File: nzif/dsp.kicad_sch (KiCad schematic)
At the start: 64 parts, among them U207 ADAU1467WBCPZ300

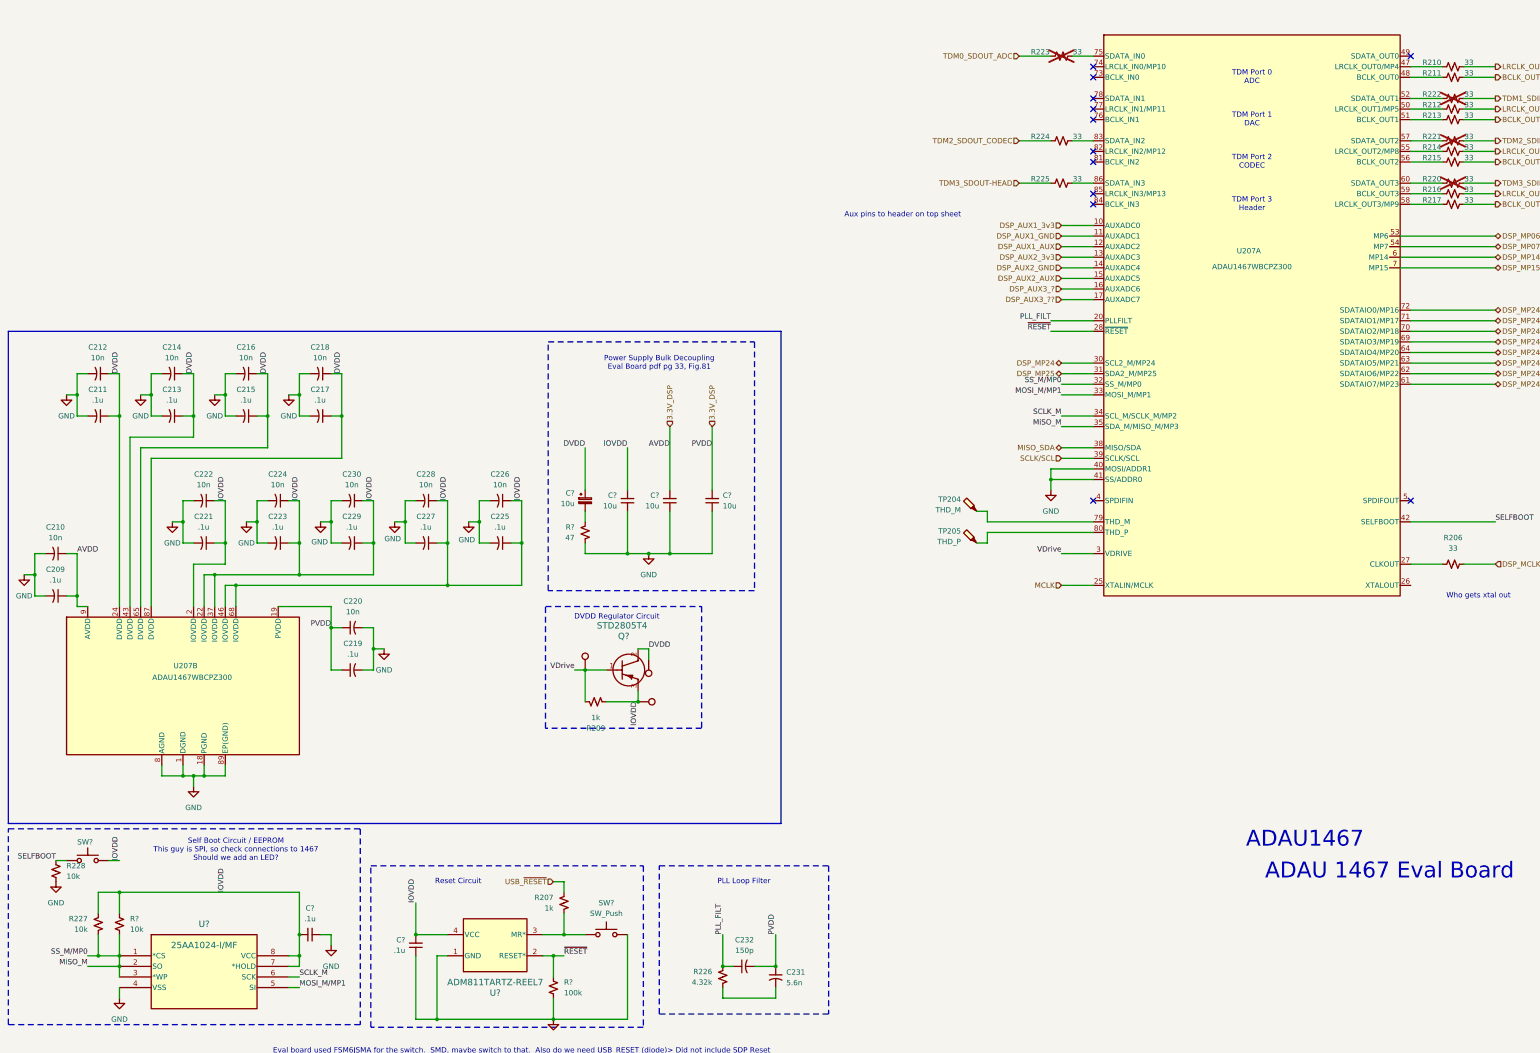
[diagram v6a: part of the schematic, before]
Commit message: updated adau1467 symbol
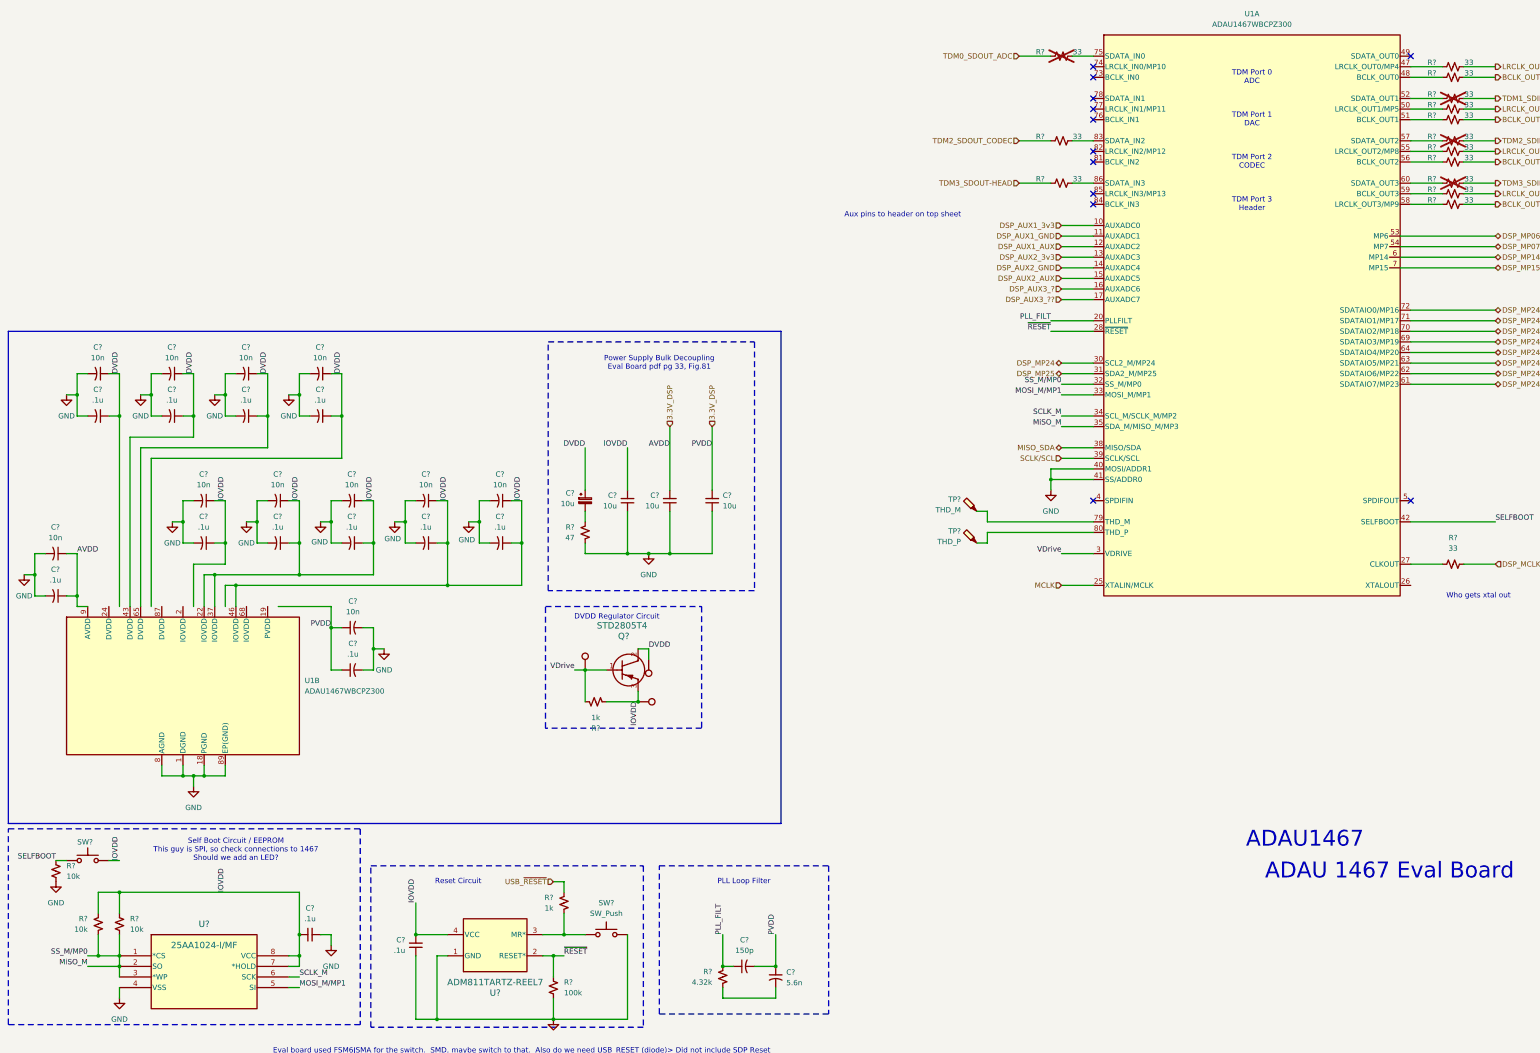
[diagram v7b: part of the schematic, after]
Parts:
- removed U207: ADAU1467WBCPZ300, nzif_footprints:CP_88_10_ADI, symbol nzif_radio_symbol_library:ADAU1467WBCPZ300
- added U1: ADAU1467WBCPZ300, nzif_footprints:CP_88_10_ADI, symbol nzif_radio_symbol_library:ADAU1467WBCPZ300
- renumbered C219 to C?, C222 to C?, C221 to C?, C210 to C?, C214 to C?, C218 to C?, C209 to C?, C231 to C?, C217 to C?, C227 to C?, C225 to C?, C220 to C?, C229 to C?, C223 to C?, C226 to C?, C213 to C?, C211 to C?, C228 to C?, C212 to C?, C215 to C?, C230 to C?, C224 to C?, C232 to C?, C216 to C?, R210 to R?, R207 to R?, R209 to R?, R217 to R?, R225 to R?, R220 to R?, R206 to R?, R224 to R?, R214 to R?, R212 to R?, R215 to R?, R221 to R?, R228 to R?, R213 to R?, R226 to R?, R222 to R?, R216 to R?, R227 to R?, R223 to R?, R211 to R?, TP204 to TP?, TP205 to TP?, TP201 to TP?, TP202 to TP?, TP203 to TP?
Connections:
- net 3.3V_DSP: now also U1.9 (AVDD)
- net DGND: now also U1.1 (DGND), U1.18 (PGND), U1.21 (DGND), U1.23 (DGND), U1.29 (DGND), U1.36 (DGND), U1.40 (MOSI/ADDR1), U1.41 (SS/ADDR0), U1.44 (DGND), U1.45 (DGND), U1.66 (DGND), U1.67 (DGND), U1.8 (AGND), U1.88 (DGND), U1.89 (EP(GND))
- net DSP_AUX1_3v3: now also U1.10 (AUXADC0)
- net DSP_AUX1_AUX: now also U1.12 (AUXADC2)
- net DSP_AUX1_GND: now also U1.11 (AUXADC1)
- net DSP_AUX2_3v3: now also U1.13 (AUXADC3)
- net DSP_AUX2_AUX: now also U1.15 (AUXADC5)
- net DSP_AUX2_GND: now also U1.14 (AUXADC4)
- net DSP_AUX3_?: now also U1.16 (AUXADC6)
- net DSP_AUX3_??: now also U1.17 (AUXADC7)
- net DSP_MP06: now also U1.53 (MP6)
- net DSP_MP07: now also U1.54 (MP7)
- net DSP_MP14: now also U1.6 (MP14)
- net DSP_MP15: now also U1.7 (MP15)
- net DSP_MP24: now also U1.30 (SCL2_M/MP24), U1.61 (SDATAIO7/MP23), U1.62 (SDATAIO6/MP22), U1.63 (SDATAIO5/MP21), U1.64 (SDATAIO4/MP20), U1.69 (SDATAIO3/MP19), U1.70 (SDATAIO2/MP18), U1.71 (SDATAIO1/MP17), U1.72 (SDATAIO0/MP16)
- net DSP_MP25: now also U1.31 (SDA2_M/MP25)
- net DVDD: now also U1.43 (DVDD), U1.65 (DVDD)
- net IOVDD: now also U1.22 (IOVDD), U1.37 (IOVDD), U1.46 (IOVDD)
- net MCLK: now also U1.25 (XTALIN/MCLK)
- net MISO_SDA: now also U1.38 (MISO/SDA)
- net MOSI_M/MP1: now also U1.33 (MOSI_M/MP1)
- net MiSO_M: now also U1.32 (SS_M/MP0), U1.35 (SDA_M/MISO_M/MP3)
- net PLL_FILT: now also U1.20 (PLLFILT)
- net SCLK_M: now also U1.34 (SCL_M/SCLK_M/MP2)
- net SCLK/SCL: now also U1.39 (SCLK/SCL)
- net SELFBOOT: now also U1.42 (SELFBOOT)
- net VDrive: now also U1.3 (VDRIVE)
- net ~{RESET}: now also U1.28 (~{RESET})
- net at R?.2: now also U1.47 (LRCLK_OUT0/MP4)
- net at R?.2: now also U1.58 (LRCLK_OUT3/MP9)
- net at R?.1: now also U1.86 (SDATA_IN3)
- net at R?.2: now also U1.60 (SDATA_OUT3)
- net at TP?.1: now also U1.79 (THD_M)
- net at R?.1: now also U1.27 (CLKOUT)
- net at R?.1: now also U1.83 (SDATA_IN2)
- net at TP?.1: now also U1.80 (THD_P)
- net at R?.2: now also U1.55 (LRCLK_OUT2/MP8)
- net at R?.2: now also U1.50 (LRCLK_OUT1/MP5)
- net at R?.2: now also U1.56 (BCLK_OUT2)
- net at R?.2: now also U1.57 (SDATA_OUT2)
- net at R?.2: now also U1.51 (BCLK_OUT1)
- net at R?.2: now also U1.52 (SDATA_OUT1)
- net at R?.2: now also U1.59 (BCLK_OUT3)
- net at R?.1: now also U1.75 (SDATA_IN0)
- net at R?.2: now also U1.48 (BCLK_OUT0)

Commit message: correct issue with unit a and b of 1467
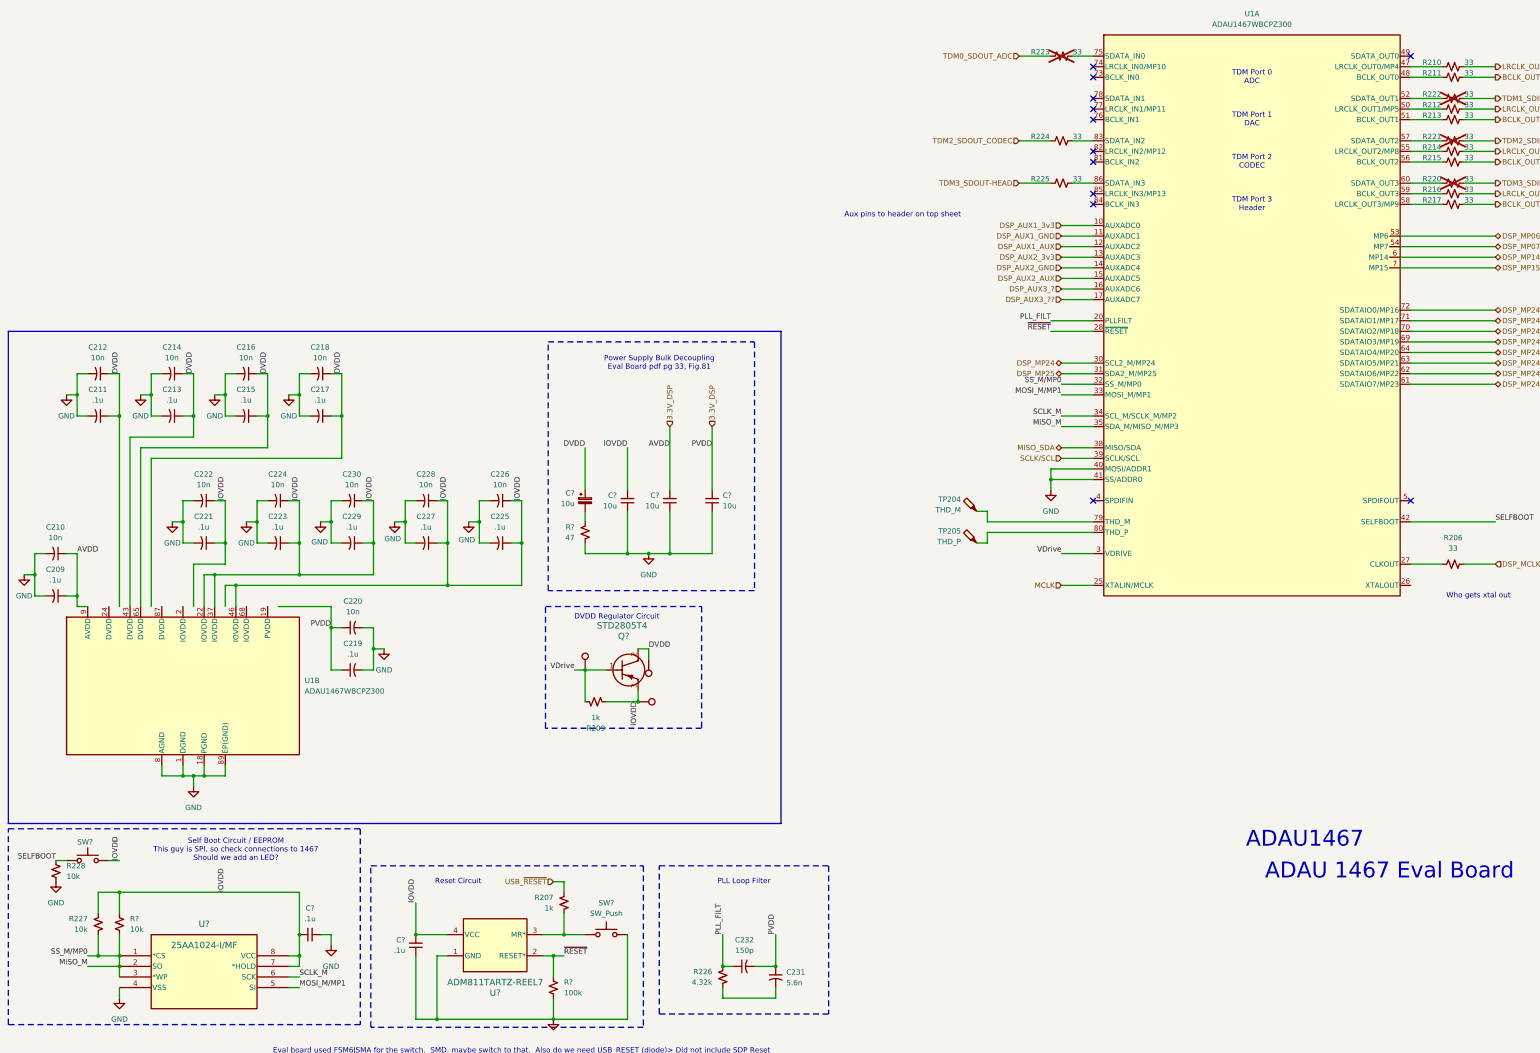
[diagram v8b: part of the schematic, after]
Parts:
- gave numbers to parts that had none: 49
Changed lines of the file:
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@@
 		(dnp no)
 		(fields_autoplaced yes)
-		(property "Reference" "C?"
+		(property "Reference" "C219"
 			(at 96.647 173.99 90)
 			(effects
@@
 		(on_board yes)
 		(dnp no)
-		(property "Reference" "R?"
+		(property "Reference" "R210"
 			(at 355.6 34.544 90)
 			(effects
@@
 		(dnp no)
 		(fields_autoplaced yes)
-		(property "Reference" "C?"
+		(property "Reference" "C222"
 			(at 60.833 133.35 90)
 			(effects
@@
 		(dnp no)
 		(fields_autoplaced yes)
-		(property "Reference" "C?"
+		(property "Reference" "C221"
 			(at 60.833 143.51 90)
 			(effects
@@
 		(on_board yes)
 		(dnp no)
-		(property "Reference" "R?"
+		(property "Reference" "R207"
 			(at 144.78 234.9499 0)
 			(effects
@@
 		(dnp no)
 		(fields_autoplaced yes)
-		(property "Reference" "#PWR?"
+		(property "Reference" "#PWR0213"
 			(at 81.28 120.65 0)
 			(effects
@@
 		(on_board yes)
 		(dnp no)
-		(property "Reference" "R?"
+		(property "Reference" "R209"
 			(at 154.94 194.31 90)
 			(effects
@@
 		(on_board yes)
 		(dnp no)
-		(property "Reference" "R?"
+		(property "Reference" "R217"
 			(at 355.6 67.564 90)
 			(effects
@@
 		(on_board yes)
 		(dnp no)
-		(property "Reference" "R?"
+		(property "Reference" "R225"
 			(at 261.62 62.484 90)
 			(effects
@@
 		(on_board yes)
 		(dnp yes)
-		(property "Reference" "R?"
+		(property "Reference" "R220"
 			(at 355.6 62.484 90)
 			(effects
@@
 		(on_board yes)
 		(dnp no)
-		(property "Reference" "TP?"
+		(property "Reference" "TP204"
 			(at 242.57 139.3824 0)
 			(effects
@@
 		(dnp no)
 		(fields_autoplaced yes)
-		(property "Reference" "C?"
+		(property "Reference" "C210"
 			(at 25.273 146.05 90)
 			(effects
@@
 		(dnp no)
 		(fields_autoplaced yes)
-		(property "Reference" "#PWR?"
+		(property "Reference" "#PWR0210"
 			(at 27.94 120.65 0)
 			(effects
@@
 		(dnp no)
 		(fields_autoplaced yes)
-		(property "Reference" "R?"
+		(property "Reference" "R206"
 			(at 360.68 148.59 90)
 			(effects
@@
 		(on_board yes)
 		(dnp no)
-		(property "Reference" "#PWR?"
+		(property "Reference" "#PWR0219"
 			(at 88.9 151.13 0)
 			(effects
@@
 		(dnp no)
 		(fields_autoplaced yes)
-		(property "Reference" "C?"
+		(property "Reference" "C214"
 			(at 53.213 102.87 90)
 			(effects
@@
 		(dnp no)
 		(fields_autoplaced yes)
-		(property "Reference" "C?"
+		(property "Reference" "C218"
 			(at 88.773 102.87 90)
 			(effects
@@
 		(dnp no)
 		(fields_autoplaced yes)
-		(property "Reference" "C?"
+		(property "Reference" "C209"
 			(at 25.273 156.21 90)
 			(effects
@@
 		(on_board yes)
 		(dnp no)
-		(property "Reference" "R?"
+		(property "Reference" "R224"
 			(at 261.62 52.324 90)
 			(effects
@@
 		(on_board yes)
 		(dnp no)
-		(property "Reference" "TP?"
+		(property "Reference" "TP205"
 			(at 242.57 147.0024 0)
 			(effects
@@
 		(dnp no)
 		(fields_autoplaced yes)
-		(property "Reference" "TP?"
+		(property "Reference" "TP201"
 			(at 154.94 175.7679 0)
 			(effects
@@
 		(dnp no)
 		(fields_autoplaced yes)
-		(property "Reference" "C?"
+		(property "Reference" "C231"
 			(at 200.66 252.8569 0)
 			(effects
@@
 		(dnp no)
 		(fields_autoplaced yes)
-		(property "Reference" "C?"
+		(property "Reference" "C217"
 			(at 88.773 113.03 90)
 			(effects
@@
 		(dnp no)
 		(fields_autoplaced yes)
-		(property "Reference" "U1"
+		(property "Reference" "U?"
 			(at 85.09 182.8799 0)
 			(effects
@@
 				)
 			)
+			(project "nzif"
+				(path "/fe42ca2f-2bb8-4d5a-9e84-807788ed632f/fa60d9db-5fbc-4f32-9a00-e3130bb41db9"
+					(reference "U?")
+					(unit 2)
+				)
+			)
 		)
 	)
@@
 		(dnp no)
 		(fields_autoplaced yes)
-		(property "Reference" "C?"
+		(property "Reference" "C227"
 			(at 114.173 143.51 90)
 			(effects
@@
 		(dnp no)
 		(fields_autoplaced yes)
-		(property "Reference" "#PWR?"
+		(property "Reference" "#PWR0212"
 			(at 63.5 120.65 0)
 			(effects
@@
 		(dnp no)
 		(fields_autoplaced yes)
-		(property "Reference" "C?"
+		(property "Reference" "C225"
 			(at 131.953 143.51 90)
 			(effects
@@
 		(on_board yes)
 		(dnp no)
-		(property "Reference" "R?"
+		(property "Reference" "R214"
 			(at 355.6 54.864 90)
 			(effects
@@
 		(dnp no)
 		(fields_autoplaced yes)
-		(property "Reference" "TP?"
+		(property "Reference" "TP202"
 			(at 169.6721 190.5 0)
 			(effects
@@
 		(on_board yes)
 		(dnp no)
-		(property "Reference" "R?"
+		(property "Reference" "R212"
 			(at 355.6 44.704 90)
 			(effects
@@
 		(on_board yes)
 		(dnp no)
-		(property "Reference" "#PWR?"
+		(property "Reference" "#PWR0217"
 			(at 124.46 151.13 0)
 			(effects
@@
 		(dnp no)
 		(fields_autoplaced yes)
-		(property "Reference" "#PWR?"
+		(property "Reference" "#PWR0215"
 			(at 53.34 151.13 0)
 			(effects
@@
 		(on_board yes)
 		(dnp no)
-		(property "Reference" "R?"
+		(property "Reference" "R215"
 			(at 355.6 57.404 90)
 			(effects
@@
 		(dnp no)
 		(fields_autoplaced yes)
-		(property "Reference" "C?"
+		(property "Reference" "C220"
 			(at 96.647 163.83 90)
 			(effects
@@
 		(on_board yes)
 		(dnp yes)
-		(property "Reference" "R?"
+		(property "Reference" "R221"
 			(at 355.6 52.324 90)
 			(effects
@@
 		(dnp no)
 		(fields_autoplaced yes)
-		(property "Reference" "C?"
+		(property "Reference" "C229"
 			(at 96.393 143.51 90)
 			(effects
@@
 		(on_board yes)
 		(dnp no)
-		(property "Reference" "R?"
+		(property "Reference" "R228"
 			(at 27.94 227.3299 0)
 			(effects
@@
 		(dnp no)
 		(fields_autoplaced yes)
-		(property "Reference" "C?"
+		(property "Reference" "C223"
 			(at 78.613 143.51 90)
 			(effects
@@
 		(on_board yes)
 		(dnp no)
-		(property "Reference" "R?"
+		(property "Reference" "R213"
 			(at 355.6 47.244 90)
 			(effects
@@
 		(on_board yes)
 		(dnp no)
-		(property "Reference" "R?"
+		(property "Reference" "R226"
 			(at 182.88 252.7299 0)
 			(effects
@@
 		(dnp no)
 		(fields_autoplaced yes)
-		(property "Reference" "C?"
+		(property "Reference" "C226"
 			(at 131.953 133.35 90)
 			(effects
@@
 		(on_board yes)
 		(dnp yes)
-		(property "Reference" "R?"
+		(property "Reference" "R222"
 			(at 355.6 42.164 90)
 			(effects
@@
 		(on_board yes)
 		(dnp no)
-		(property "Reference" "R?"
+		(property "Reference" "R216"
 			(at 355.6 65.024 90)
 			(effects
@@
 		(on_board yes)
 		(dnp no)
-		(property "Reference" "R?"
+		(property "Reference" "R227"
 			(at 33.02 240.0299 0)
 			(effects
@@
 		(dnp no)
 		(fields_autoplaced yes)
-		(property "Reference" "C?"
+		(property "Reference" "C213"
 			(at 53.213 113.03 90)
 			(effects
@@
 		(dnp no)
 		(fields_autoplaced yes)
-		(property "Reference" "C?"
+		(property "Reference" "C211"
 			(at 35.433 113.03 90)
 			(effects
@@
 		(dnp no)
 		(fields_autoplaced yes)
-		(property "Reference" "#PWR?"
+		(property "Reference" "#PWR0216"
 			(at 71.12 151.13 0)
 			(effects
@@
 		(on_board yes)
 		(dnp yes)
-		(property "Reference" "R?"
+		(property "Reference" "R223"
 			(at 261.62 32.004 90)
 			(effects
@@
 		(dnp no)
 		(fields_autoplaced yes)
-		(property "Reference" "C?"
+		(property "Reference" "C228"
 			(at 114.173 133.35 90)
 			(effects
@@
 		(dnp no)
 		(fields_autoplaced yes)
-		(property "Reference" "C?"
+		(property "Reference" "C212"
 			(at 35.433 102.87 90)
 			(effects
@@
 		(dnp no)
 		(fields_autoplaced yes)
-		(property "Reference" "C?"
+		(property "Reference" "C215"
 			(at 70.993 113.03 90)
 			(effects
@@
 		(on_board yes)
 		(dnp no)
-		(property "Reference" "R?"
+		(property "Reference" "R211"
 			(at 355.6 37.084 90)
 			(effects
@@
 		(dnp no)
 		(fields_autoplaced yes)
-		(property "Reference" "C?"
+		(property "Reference" "C230"
 			(at 96.393 133.35 90)
 			(effects
@@
 		(dnp no)
 		(fields_autoplaced yes)
-		(property "Reference" "#PWR?"
+		(property "Reference" "#PWR0211"
 			(at 45.72 120.65 0)
 			(effects
@@
 		(dnp no)
 		(fields_autoplaced yes)
-		(property "Reference" "#PWR?"
+		(property "Reference" "#PWR0209"
 			(at 17.78 163.83 0)
 			(effects
@@
 		(dnp no)
 		(fields_autoplaced yes)
-		(property "Reference" "C?"
+		(property "Reference" "C224"
 			(at 78.613 133.35 90)
 			(effects
@@
 		(dnp no)
 		(fields_autoplaced yes)
-		(property "Reference" "#PWR?"
+		(property "Reference" "#PWR0249"
 			(at 264.16 143.51 0)
 			(effects
@@
 		(dnp no)
 		(fields_autoplaced yes)
-		(property "Reference" "C?"
+		(property "Reference" "C232"
 			(at 190.627 245.11 90)
 			(effects
@@
 		(dnp no)
 		(fields_autoplaced yes)
-		(property "Reference" "#PWR?"
+		(property "Reference" "#PWR0214"
 			(at 104.14 181.61 0)
 			(effects
@@
 		(dnp no)
 		(fields_autoplaced yes)
-		(property "Reference" "C?"
+		(property "Reference" "C216"
 			(at 70.993 102.87 90)
 			(effects
@@
 		(on_board yes)
 		(dnp no)
-		(property "Reference" "#PWR?"
+		(property "Reference" "#PWR0208"
 			(at 58.42 214.63 0)
 			(effects
@@
 		(on_board yes)
 		(dnp no)
-		(property "Reference" "#PWR?"
+		(property "Reference" "#PWR0218"
 			(at 106.68 151.13 0)
 			(effects
@@
 		(dnp no)
 		(fields_autoplaced yes)
-		(property "Reference" "#PWR?"
+		(property "Reference" "#PWR0220"
 			(at 25.4 237.49 0)
 			(effects
@@
 		(dnp no)
 		(fields_autoplaced yes)
-		(property "Reference" "U1"
+		(property "Reference" "U?"
 			(at 312.42 22.86 0)
 			(effects
@@
 				)
 			)
+			(project "nzif"
+				(path "/fe42ca2f-2bb8-4d5a-9e84-807788ed632f/fa60d9db-5fbc-4f32-9a00-e3130bb41db9"
+					(reference "U?")
+					(unit 1)
+				)
+			)
 		)
 	)
@@
 		(dnp no)
 		(fields_autoplaced yes)
-		(property "Reference" "TP?"
+		(property "Reference" "TP203"
 			(at 165.1 182.3721 0)
 			(effects
